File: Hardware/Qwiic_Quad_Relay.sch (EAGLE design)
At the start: 65 parts, among them J2 Qwiic Right Angle, J3 Qwiic Right Angle, J4 AVR_SPI_PROG_3X2TESTPOINTS, J9 POWER_JACK, K1 RELAY-SPDT-JZC-11F, K2 RELAY-SPDT-JZC-11F, K3 RELAY-SPDT-JZC-11F, K4 RELAY-SPDT-JZC-11F, Q1 600mA/40V, Q2 600mA/40V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

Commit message: Adds circuitry for DC-DC converter (no traces routed)
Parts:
- removed FRAME1: FRAME-LETTER, SparkFun-Aesthetics:FRAME-LETTER
- removed R6: 240, SparkFun-Resistors:240OHM-0603-1/10W-1%
- removed R7: 715, SparkFun-Resistors:715OHM-0603-1/10W-1%
- added FRAME2: FRAME-LEDGER, SparkFun-Aesthetics:FRAME-LEDGER
- U1: value (none) -> LMR14010A; device SparkFun-IC-Power:V_REG_LM1117SOT223 -> SparkFun-IC-Power:LMR14010A
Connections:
- removed net N$19: R6.1, R7.2, U1.ADJ
- net 5V: no longer R6.2, U1.OUT
- net GND: no longer R7.1
- net N$4: no longer U1.IN
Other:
- moved on the sheet: C1, C2, C3, C4, D1, D11, D2, D3, D4, D5, D6, D7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

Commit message: Re-adds dc-dc converter circuitry - somehow it was not in the last push
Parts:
- removed JP10: JUMPER-SMT_2_NO_SILK, SparkFun-Jumpers:JUMPER-SMT_2_NO_SILK
- added ADDR, LED: JUMPER-SMT_2_NO_SILK, SparkFun-Jumpers:JUMPER-SMT_2_NO_SILK
- added C5: 0.1uF, SparkFun-Capacitors:0.1UF-0402-10V-10%-X7R
- added D10: 3A/10V/280mV, SparkFun-DiscreteSemi:DIODE-SCHOTTKY-BAT60A
- added L1: 15uH, SparkFun-Coils:INDUCTOR-LHQ32-15UH
- added R6: 20k, SparkFun-Resistors:20KOHM-0603-1/10W-1%
- added R7: 100k, SparkFun-Resistors:100KOHM-0603-1/10W-1%
- C3: value 0.1uF -> 10uF; device SparkFun-Capacitors:0.1UF-0603-25V-(+80/-20%) -> SparkFun-Capacitors:10UF-0603-6.3V-20%
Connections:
- new net N$1: C5.1, U1.CB
- new net N$14: LED.2, R9.2
- new net N$16: R6.2, R7.1, U1.FB
- new net N$7: C5.2, D10.C, L1.1, U1.SW
- net 5V: now also L1.2, R7.2
- net ADDR_JUMP: now also ADDR.1; no longer JP10.1
- net GND: now also ADDR.2, D10.A, LED.1, R6.1, U1.GND; no longer JP10.2, R9.2
- net N$4: now also U1.SHDN, U1.VIN
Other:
- note added: "111K"
- note added: "Cut jumper to disable LED."
- note added: "Jumpers"
- moved on the sheet: C1, C2, C3, C4, D1, D11, D2, D3, D4, D5, D6, D7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

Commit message: Routes new circuitry
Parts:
- removed JP7: JUMPER-SMT_2_NO_SILK, SparkFun-Jumpers:JUMPER-SMT_2_NO_SILK
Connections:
- net N$1 renamed CB
- net N$16 renamed FB
- net N$4 renamed VIN_DC_DC
- net N$7 renamed SW
- removed net N$20: D9.C, R17.2
- removed net N$21: D8.C, R16.2
- removed net N$22: D7.C, R15.2
- new net N$1: D2.A, R4.1
- new net N$4: D7.A, R15.1
- new net N$7: D8.A, R16.1
- net 5V: now also R15.2, R16.2, R17.2, R4.2; no longer D2.A, D7.A, D8.A, D9.A, JP7.2
- net N$12: now also D7.C; no longer R15.1
- net N$15: now also D8.C; no longer R16.1
- net N$17: now also D9.C; no longer R17.1
- net N$2: now also D2.C; no longer R4.1
- net N$8: now also D9.A, R17.1; no longer D2.C, R4.2
- net VIN: no longer JP7.1
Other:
- note added: "v20"
- note removed: "Close Jumper to Bypass Voltage Regulator only if using 5V Power Supply"
- note removed: "v10"
- moved on the sheet: D2, D7, D8, D9, R15, R16, R17, R4

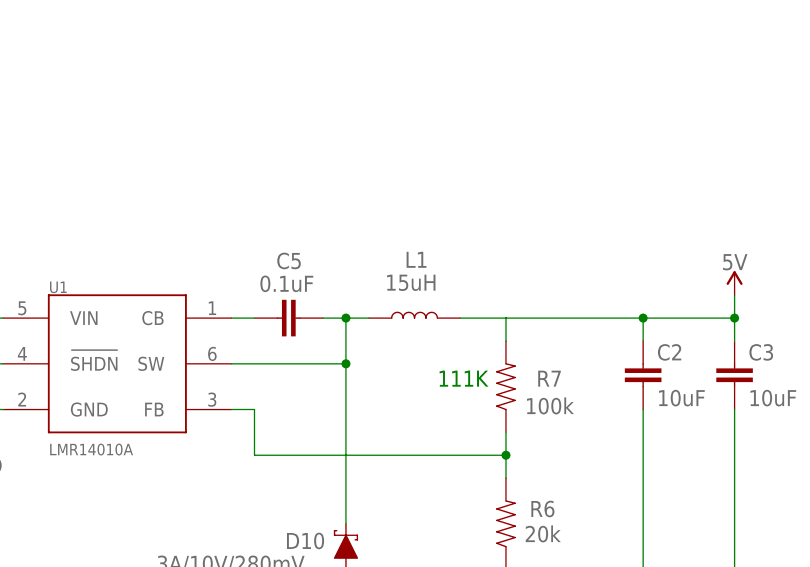
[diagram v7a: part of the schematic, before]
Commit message: Updates inductor with inductor with correct amperage rating
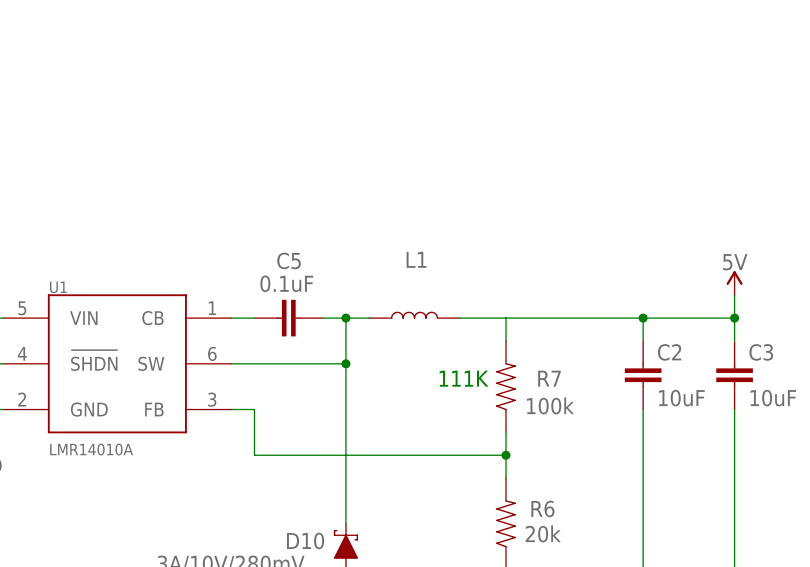
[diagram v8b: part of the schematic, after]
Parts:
- L1: device SparkFun-Coils:INDUCTOR-LHQ32-15UH -> SparkFun-Coils:INDUCTOR-DEM-2818C-15UH
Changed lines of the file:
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@@
 <part name="GND20" library="SparkFun-PowerSymbols" deviceset="GND" device=""/>
 <part name="C5" library="SparkFun-Capacitors" deviceset="0.1UF" device="-0402-10V-10%-X7R" value="0.1uF"/>
-<part name="L1" library="SparkFun-Coils" deviceset="INDUCTOR" device="-LHQ32-15UH" value="15uH"/>
+<part name="L1" library="SparkFun-Coils" deviceset="INDUCTOR" device="-DEM-2818C-15UH" value="15uH"/>
 <part name="R6" library="SparkFun-Resistors" deviceset="20KOHM" device="-0603-1/10W-1%" value="20k"/>
 <part name="R7" library="SparkFun-Resistors" deviceset="100KOHM" device="-0603-1/10W-1%" value="100k"/>
@@
 <instance part="L1" gate="G$1" x="365.76" y="149.86" smashed="yes" rot="R90">
 <attribute name="NAME" x="367.284" y="157.226" size="1.778" layer="95" font="vector" rot="R180"/>
-<attribute name="VALUE" x="368.3" y="152.908" size="1.778" layer="96" font="vector" rot="R180" align="top-left"/>
 </instance>
 <instance part="R6" gate="G$1" x="375.92" y="127" smashed="yes" rot="R90">
